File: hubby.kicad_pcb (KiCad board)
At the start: 2 copper layers, 70 x 100 mm, 79 parts, among them IC1 FE2.1, J1 USB1, J10 VPROG_OUT, J11 1V8_OUT, J12 VPROG_OUT, J13 USB2, J14 USB2, J15 UART_OUT, J17 EXT_PS_OUT, J18 EXT_PS_OUT, J2 USB2, J5 3V3_OUT, J6 1V8_OUT, J7 5V_OUT, J8 5V_OUT, J9 3V3_OUT, P1 USB_C_Plug_USB2.0, Q1 AO3401A, Q2 AO3401A, Q3 AO3401A, U1 USBLC6-2SC6, U10 TPS565208, U12 TPS565208, U13 AP1117-18, U14 AP1117-33, U15 USBLC6-2SC6, U16 USBLC6-2SC6, U17 USBLC6-2SC6, U18 USBLC6-2SC6, U19 INA181, U2 STM32F103RBTx, U3 INA181, U4 INA181, U5 INA181, U6 INA181, U7 FT2232HL, U8 INA181, U9 INA181, X1 ECS-2520MV-xxx-xx

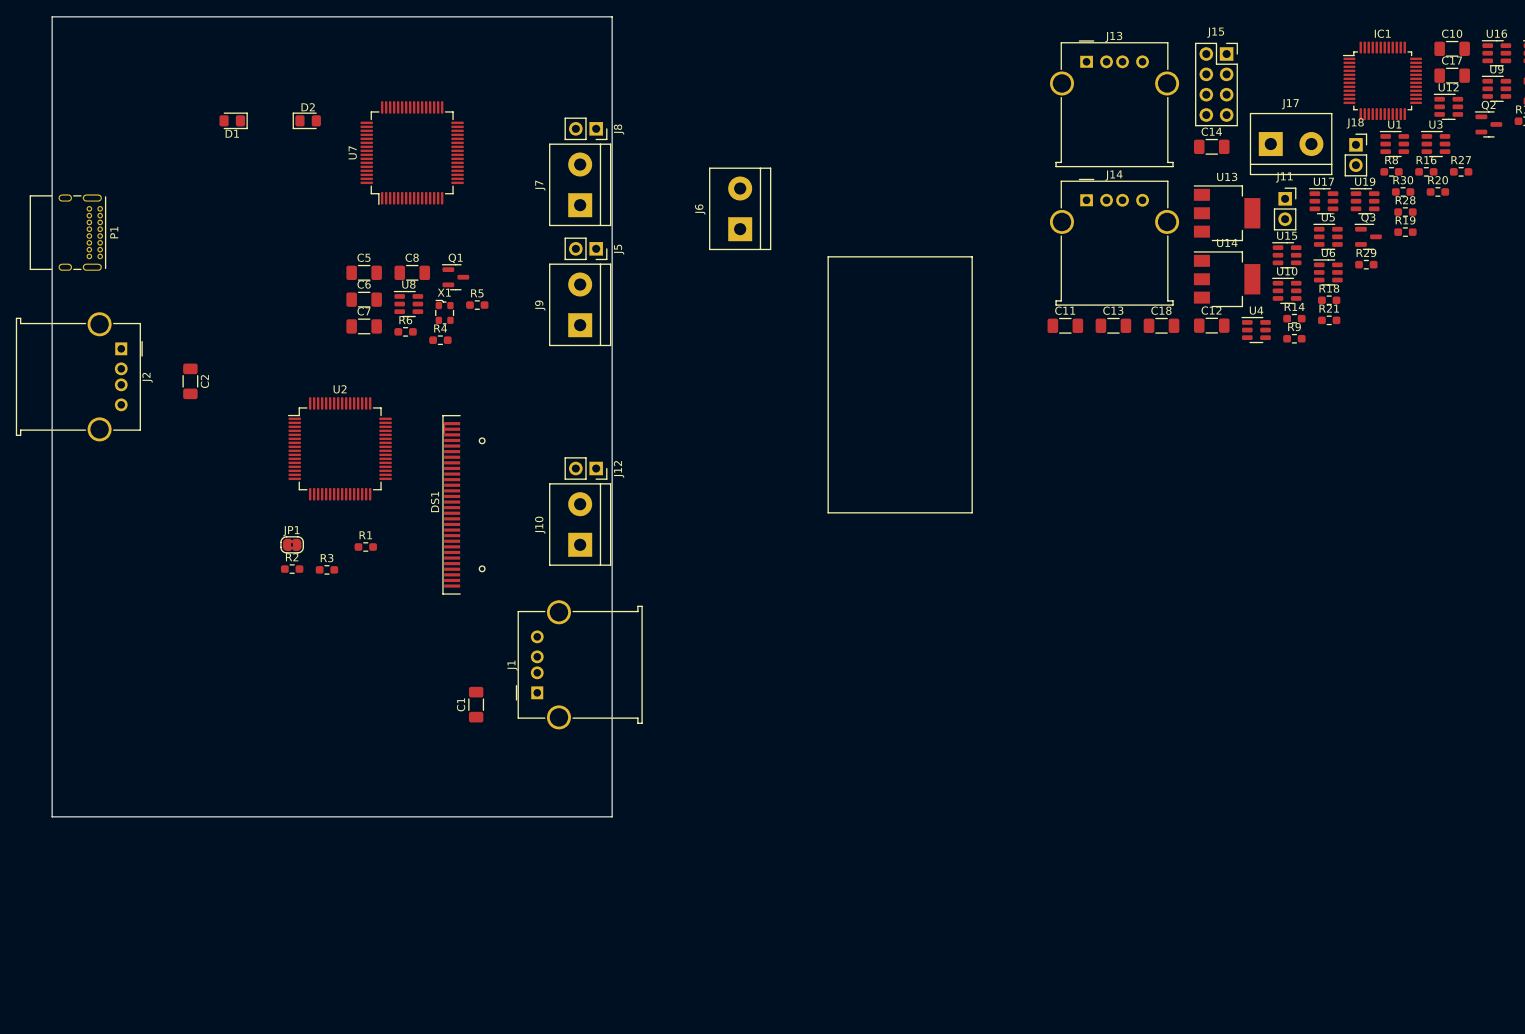
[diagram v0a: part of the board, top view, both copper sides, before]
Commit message: commiting cause i'm terrified of kicad 5.99
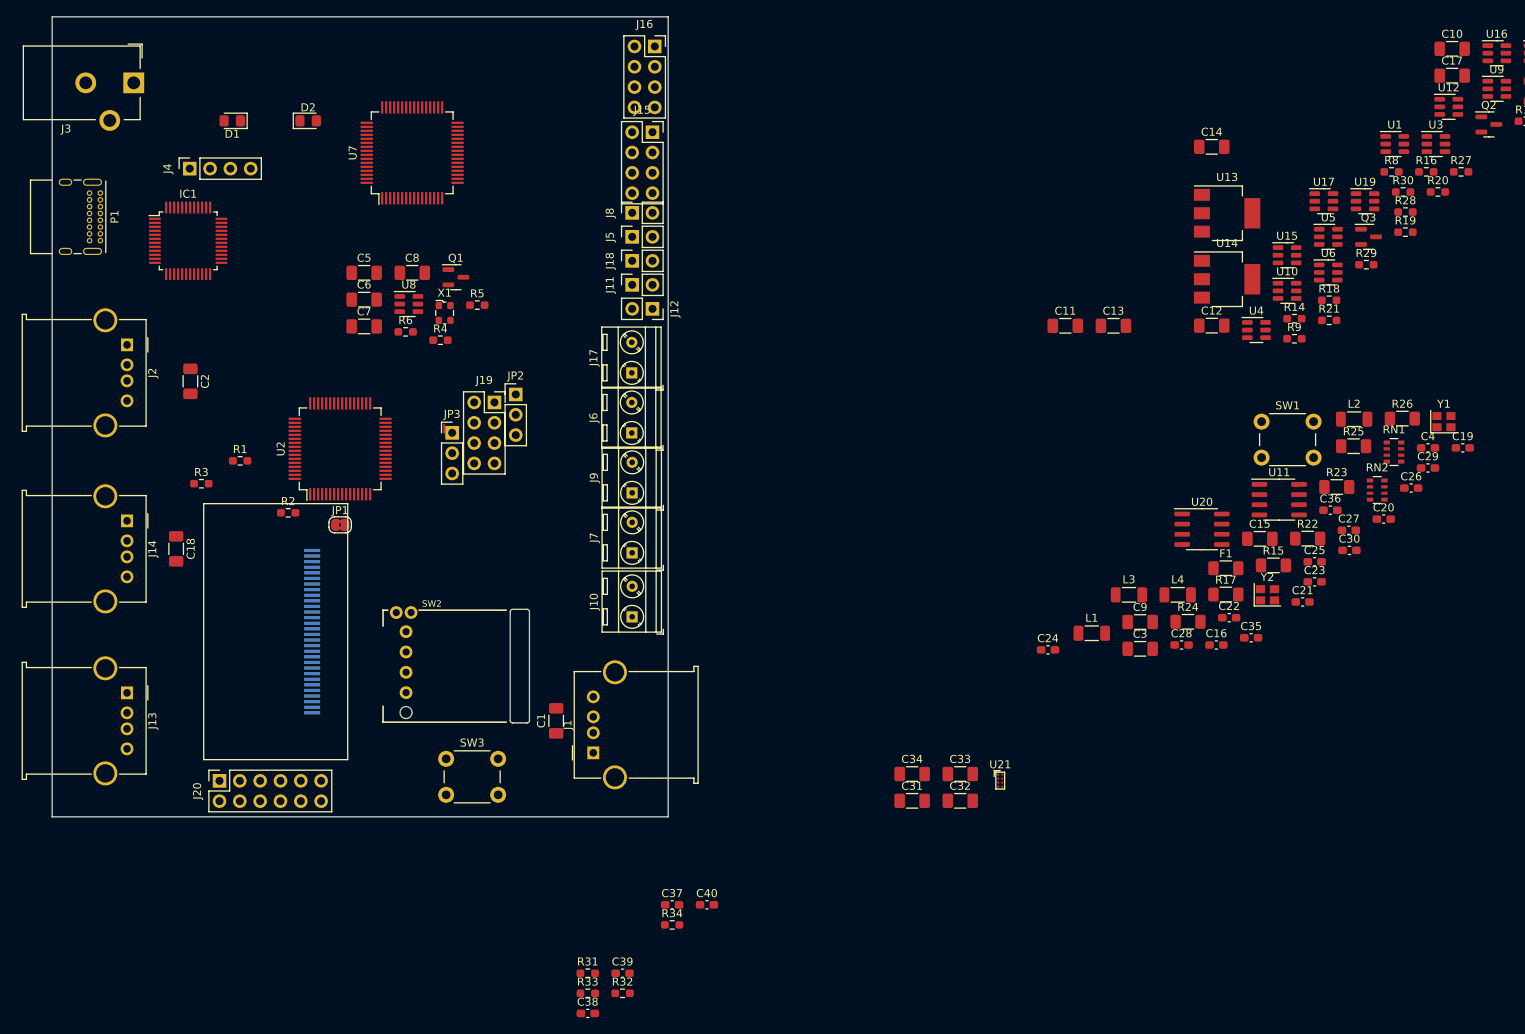
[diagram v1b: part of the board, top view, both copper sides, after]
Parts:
- added C15: C, Capacitor_SMD:C_1206_3216Metric_Pad1.33x1.80mm_HandSolder, F.Cu at (251.0, 95.2)
- added C16: 100n, Capacitor_SMD:C_0603_1608Metric_Pad1.08x0.95mm_HandSolder, F.Cu at (245.5, 108.5)
- added C19: 100n, Capacitor_SMD:C_0603_1608Metric_Pad1.08x0.95mm_HandSolder, F.Cu at (276.3, 83.9)
- added C20: 100n, Capacitor_SMD:C_0603_1608Metric_Pad1.08x0.95mm_HandSolder, F.Cu at (266.4, 92.8)
- added C21: 100n, Capacitor_SMD:C_0603_1608Metric_Pad1.08x0.95mm_HandSolder, F.Cu at (256.3, 103.1)
- added C22: 100n, Capacitor_SMD:C_0603_1608Metric_Pad1.08x0.95mm_HandSolder, F.Cu at (247.1, 105.1)
- added C23: 100n, Capacitor_SMD:C_0603_1608Metric_Pad1.08x0.95mm_HandSolder, F.Cu at (257.8, 100.6)
- added C24: 100n, Capacitor_SMD:C_0603_1608Metric_Pad1.08x0.95mm_HandSolder, F.Cu at (224.5, 109.1)
- added C25: 100n, Capacitor_SMD:C_0603_1608Metric_Pad1.08x0.95mm_HandSolder, F.Cu at (257.8, 98.1)
- added C26: 100n, Capacitor_SMD:C_0603_1608Metric_Pad1.08x0.95mm_HandSolder, F.Cu at (269.9, 88.9)
- added C27: 100n, Capacitor_SMD:C_0603_1608Metric_Pad1.08x0.95mm_HandSolder, F.Cu at (262.1, 94.2)
- added C28: 100n, Capacitor_SMD:C_0603_1608Metric_Pad1.08x0.95mm_HandSolder, F.Cu at (241.2, 108.5)
- added C29: 1n, Capacitor_SMD:C_0603_1608Metric_Pad1.08x0.95mm_HandSolder, F.Cu at (272.0, 86.4)
- added C3: C, Capacitor_SMD:C_1206_3216Metric_Pad1.33x1.80mm_HandSolder, F.Cu at (236.0, 109.0)
- added C30: 1n, Capacitor_SMD:C_0603_1608Metric_Pad1.08x0.95mm_HandSolder, F.Cu at (262.2, 96.7)
- added C31: 10u, Capacitor_SMD:C_1206_3216Metric_Pad1.33x1.80mm_HandSolder, F.Cu at (207.5, 128.0)
- added C32: 10u, Capacitor_SMD:C_1206_3216Metric_Pad1.33x1.80mm_HandSolder, F.Cu at (213.5, 128.0)
- added C33: 10u, Capacitor_SMD:C_1206_3216Metric_Pad1.33x1.80mm_HandSolder, F.Cu at (213.5, 124.7)
- added C34: 10u, Capacitor_SMD:C_1206_3216Metric_Pad1.33x1.80mm_HandSolder, F.Cu at (207.5, 124.7)
- added C35: 100n, Capacitor_SMD:C_0603_1608Metric_Pad1.08x0.95mm_HandSolder, F.Cu at (249.9, 107.6)
- added C36: 100n, Capacitor_SMD:C_0603_1608Metric_Pad1.08x0.95mm_HandSolder, F.Cu at (259.8, 91.7)
- added C37: 1n, Capacitor_SMD:C_0603_1608Metric_Pad1.08x0.95mm_HandSolder, F.Cu at (177.5, 141.0)
- added C38: 1n, Capacitor_SMD:C_0603_1608Metric_Pad1.08x0.95mm_HandSolder, F.Cu at (166.9, 154.6)
- added C39: 1n, Capacitor_SMD:C_0603_1608Metric_Pad1.08x0.95mm_HandSolder, F.Cu at (171.3, 149.6)
- added C4: 100n, Capacitor_SMD:C_0603_1608Metric_Pad1.08x0.95mm_HandSolder, F.Cu at (272.0, 83.9)
- added C40: 1n, Capacitor_SMD:C_0603_1608Metric_Pad1.08x0.95mm_HandSolder, F.Cu at (181.8, 141.0)
- added C9: C, Capacitor_SMD:C_1206_3216Metric_Pad1.33x1.80mm_HandSolder, F.Cu at (236.0, 105.7)
- added F1: Polyfuse, Resistor_SMD:R_1206_3216Metric_Pad1.30x1.75mm_HandSolder, F.Cu at (246.7, 98.9)
- added J16: JTAG_OUT, Connector_PinSocket_2.54mm:PinSocket_2x04_P2.54mm_Vertical, F.Cu at (175.3, 33.7)
- added J19: STM_PROG_ENA, Connector_PinSocket_2.54mm:PinSocket_2x04_P2.54mm_Vertical, F.Cu at (155.3, 78.2)
- added J20: STM_EXT_IO, Connector_PinSocket_2.54mm:PinSocket_2x06_P2.54mm_Vertical, F.Cu at (120.9, 125.5)
- added J3: Barrel_Jack_Switch, Connector_BarrelJack:BarrelJack_CUI_PJ-102AH_Horizontal, F.Cu at (110.2, 38.2)
- added J4: Conn_01x04, Connector_PinSocket_2.54mm:PinSocket_1x04_P2.54mm_Vertical, F.Cu at (117.2, 49.0)
- added JP2: TDO_VSHIFT, Connector_PinHeader_2.54mm:PinHeader_1x03_P2.54mm_Vertical, F.Cu at (157.9, 77.2)
- added JP3: RXD_VSHIFT, Connector_PinHeader_2.54mm:PinHeader_1x03_P2.54mm_Vertical, F.Cu at (150.0, 82.0)
- added L1: L, Inductor_SMD:L_1206_3216Metric_Pad1.22x1.90mm_HandSolder, F.Cu at (229.9, 107.0)
- added L2: L, Inductor_SMD:L_1206_3216Metric_Pad1.22x1.90mm_HandSolder, F.Cu at (262.8, 80.3)
- added L3: L, Inductor_SMD:L_1206_3216Metric_Pad1.22x1.90mm_HandSolder, F.Cu at (234.6, 102.2)
- added L4: L, Inductor_SMD:L_1206_3216Metric_Pad1.22x1.90mm_HandSolder, F.Cu at (240.7, 102.2)
- added R15: 0.5R, Resistor_SMD:R_1206_3216Metric_Pad1.30x1.75mm_HandSolder, F.Cu at (252.7, 98.6)
- added R17: 0.5R, Resistor_SMD:R_1206_3216Metric_Pad1.30x1.75mm_HandSolder, F.Cu at (246.7, 102.2)
- added R22: 0.5R, Resistor_SMD:R_1206_3216Metric_Pad1.30x1.75mm_HandSolder, F.Cu at (256.9, 95.2)
- added R23: 0.5R, Resistor_SMD:R_1206_3216Metric_Pad1.30x1.75mm_HandSolder, F.Cu at (260.6, 88.8)
- added R24: 0.5R, Resistor_SMD:R_1206_3216Metric_Pad1.30x1.75mm_HandSolder, F.Cu at (242.0, 105.6)
- added R25: 0.5R, Resistor_SMD:R_1206_3216Metric_Pad1.30x1.75mm_HandSolder, F.Cu at (262.7, 83.7)
- added R26: 0.5R, Resistor_SMD:R_1206_3216Metric_Pad1.30x1.75mm_HandSolder, F.Cu at (268.8, 80.2)
- added R31: 100k, Resistor_SMD:R_0603_1608Metric_Pad0.98x0.95mm_HandSolder, F.Cu at (166.9, 149.6)
- added R32: 100k, Resistor_SMD:R_0603_1608Metric_Pad0.98x0.95mm_HandSolder, F.Cu at (171.3, 152.1)
- added R33: 100k, Resistor_SMD:R_0603_1608Metric_Pad0.98x0.95mm_HandSolder, F.Cu at (166.9, 152.1)
- added R34: 100k, Resistor_SMD:R_0603_1608Metric_Pad0.98x0.95mm_HandSolder, F.Cu at (177.5, 143.5)
- added RN1: 22, Resistor_SMD:R_Array_Convex_4x0603, F.Cu at (267.7, 84.4)
- added RN2: 22, Resistor_SMD:R_Array_Convex_4x0603, F.Cu at (265.6, 89.2)
- added SW1: SW_Push, Button_Switch_THT:SW_PUSH_6mm_H4.3mm, F.Cu at (251.2, 80.6)
- added SW2: KB_ENC, Critbit_lib:RollerEncoder_Panasonic_EVQWGD001, F.Cu at (149.9, 110.7)
- added SW3: BUT_BACK, Button_Switch_THT:SW_PUSH_6mm_H4.3mm, F.Cu at (149.2, 122.8)
- added U11: 24LC00, Package_SO:SOIC-8_3.9x4.9mm_P1.27mm, F.Cu at (253.4, 90.3)
- added U20: 24LC00, Package_SO:SOIC-8_3.9x4.9mm_P1.27mm, F.Cu at (243.7, 94.0)
- added U21: SN74LVC2T45YZP, Package_BGA:Texas_DSBGA-8_0.9x1.9mm_Layout2x4_P0.5mm, F.Cu at (218.5, 125.5)
- added Y1: 6MHZ 2520, Crystal:Crystal_SMD_2520-4Pin_2.5x2.0mm, F.Cu at (274.0, 80.6)
- added Y2: 6MHZ 2520, Crystal:Crystal_SMD_2520-4Pin_2.5x2.0mm, F.Cu at (251.9, 102.2)
- DS1: moved to B.Cu
- J10, J17, J6, J7, J9: footprint TerminalBlock:TerminalBlock_bornier-2_P5.08mm -> TerminalBlock_MetzConnect:TerminalBlock_MetzConnect_Type086_RT03402HBLC_1x02_P3.81mm_Horizontal
- moved IC1 150.7 mm to (117.0, 58.0)
- moved J13 143.6 mm to (109.4, 114.5), turned to -90 degrees
- moved J14 126.5 mm to (109.4, 93.0), turned to -90 degrees
- moved C18 126.3 mm to (115.5, 96.5), turned to -90 degrees
- moved J18 91.6 mm to (172.5, 60.5), turned to 90 degrees
- moved J17 84.8 mm to (172.5, 74.5), turned to 90 degrees
- moved J11 82.3 mm to (172.5, 63.5), turned to 90 degrees
- moved J15 72.4 mm to (175.0, 44.4)
- moved J7 43.9 mm to (172.5, 97.0)
- moved J6 28.9 mm to (172.5, 82.0)
- moved DS1 23.6 mm to (132.5, 106.8), turned to 90 degrees
- moved J9 21.9 mm to (172.5, 89.5)
- moved J12 21.2 mm to (175.0, 66.5)
- moved R1 19.0 mm to (123.5, 85.5)
- moved R3 19.0 mm to (118.7, 88.4)
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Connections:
- IC1 pad 22: unconnected-(IC1-Pad22) -> Net-(C31-Pad1)
- IC1 pad 23: unconnected-(IC1-Pad23) -> Net-(C32-Pad1)
- J15 pad 2: /RTS -> /TARG_RTS
- J15 pad 3: /DTR -> /TARG_DTR
- J15 pad 4: /RXD -> /TARG_TXD
- J15 pad 8: /TXD -> /TARG_RXD
- JP1 pad 1: /TDI -> /TDO
- R2 pad 2: /TDO -> /TDI
- U2 pad 10: unconnected-(U2-Pad10) -> /ADC_???
- U2 pad 12: Net-(U2-Pad12) -> GND
- U2 pad 18: Net-(U2-Pad12) -> GND
- U2 pad 24: unconnected-(U2-Pad24) -> /STM_PROBE1
- U2 pad 25: unconnected-(U2-Pad25) -> /STM_PROBE2
- U2 pad 26: /5V_CURR -> /EXT_IO1
- U2 pad 27: unconnected-(U2-Pad27) -> /EXT_IO2
- U2 pad 28: unconnected-(U2-Pad28) -> /EXT_IO3
- U2 pad 29: unconnected-(U2-Pad29) -> /EXT_IO4
- U2 pad 30: unconnected-(U2-Pad30) -> /EXT_IO5
- U2 pad 31: Net-(U2-Pad12) -> GND
- U2 pad 37: unconnected-(U2-Pad37) -> /VPROG_PWM
- U2 pad 41: /VPROG_PWM -> /STM32_CLK_OUT
- U2 pad 42: unconnected-(U2-Pad42) -> /STM_TXD
- U2 pad 43: unconnected-(U2-Pad43) -> /STM_RXD
- U2 pad 44: unconnected-(U2-Pad44) -> /STM32_DM
- U2 pad 45: unconnected-(U2-Pad45) -> /STM32_DP
- U2 pad 47: Net-(U2-Pad12) -> GND
- U2 pad 5: unconnected-(U2-Pad5) -> /STM32_12MHZ
- U2 pad 50: unconnected-(U2-Pad50) -> /STM_PULSE_CNT
- U2 pad 54: unconnected-(U2-Pad54) -> /OLED_RST
- U2 pad 55: unconnected-(U2-Pad55) -> /OLED_CLK
- U2 pad 56: unconnected-(U2-Pad56) -> /OLED_CS
- U2 pad 57: unconnected-(U2-Pad57) -> /OLED_MOSI
- U2 pad 58: unconnected-(U2-Pad58) -> /ENC_A
- U2 pad 59: unconnected-(U2-Pad59) -> /ENC_B
- U2 pad 60: unconnected-(U2-Pad60) -> GND
- U2 pad 61: unconnected-(U2-Pad61) -> /ENC_BUT
- U2 pad 62: unconnected-(U2-Pad62) -> /STM_BUT_BACK
- U2 pad 63: Net-(U2-Pad12) -> GND
- U2 pad 7: unconnected-(U2-Pad7) -> /STM_BUT_RST
- U2 pad 8: unconnected-(U2-Pad8) -> /5V_CURR
- U2 pad 9: unconnected-(U2-Pad9) -> /USB1_CURR
- U7 pad 2: unconnected-(U7-Pad2) -> Net-(C33-Pad1)
- U7 pad 3: unconnected-(U7-Pad3) -> Net-(C34-Pad1)
- U7 pad 4: Net-(U7-Pad4) -> Net-(C26-Pad1)
- U7 pad 9: Net-(U7-Pad4) -> Net-(C35-Pad1)
- X1 pad 2: unconnected-(X1-Pad2) -> GND
- X1 pad 3: unconnected-(X1-Pad3) -> /STM32_12MHZ
- X1 pad 4: unconnected-(X1-Pad4) -> +3V3
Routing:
- net Net-(C5-Pad1): track 1.00 -> 0.00 mm
- net GND: track 0.00 -> 1.00 mm
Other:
- board size 70 x 100 mm -> 77 x 100 mm
- board text added: "target stackup - JLC7628 HI-SPD1 0.2 mm GND 0.465 mm HI-SPD2/PWR 0.2 mm LO-SPD USB 90R: OUT - .7mm/.4mm IN - .5/.4mm"

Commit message: another progress checkpoint
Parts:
- removed DS1: OLED-128O064D, Display:OLED-128O064D
- removed J10: VPROG_OUT, TerminalBlock_MetzConnect:TerminalBlock_MetzConnect_Type086_RT03402HBLC_1x02_P3.81mm_Horizontal
- removed J11: 1V8_OUT, Connector_PinSocket_2.54mm:PinSocket_1x02_P2.54mm_Vertical
- removed J12: VPROG_OUT, Connector_PinSocket_2.54mm:PinSocket_1x02_P2.54mm_Vertical
- removed J15: UART_OUT, Connector_PinSocket_2.54mm:PinSocket_2x04_P2.54mm_Vertical
- removed J17: EXT_PS_OUT, TerminalBlock_MetzConnect:TerminalBlock_MetzConnect_Type086_RT03402HBLC_1x02_P3.81mm_Horizontal
- removed J18: EXT_PS_OUT, Connector_PinSocket_2.54mm:PinSocket_1x02_P2.54mm_Vertical
- removed J8: 5V_OUT, Connector_PinSocket_2.54mm:PinSocket_1x02_P2.54mm_Vertical
- removed J9: 3V3_OUT, TerminalBlock_MetzConnect:TerminalBlock_MetzConnect_Type086_RT03402HBLC_1x02_P3.81mm_Horizontal
- added C41: 10u/16V, Capacitor_SMD:C_1206_3216Metric_Pad1.33x1.80mm_HandSolder, F.Cu at (198.0, 50.5)
- added C42: 220u, Capacitor_THT:C_Radial_D10.0mm_H12.5mm_P5.00mm, F.Cu at (161.2, 47.0)
- added C43: 1n, Capacitor_SMD:C_0603_1608Metric_Pad1.08x0.95mm_HandSolder, F.Cu at (117.0, 154.0)
- added C44: 1n, Capacitor_SMD:C_0603_1608Metric_Pad1.08x0.95mm_HandSolder, F.Cu at (112.7, 159.0)
- added C45: 10u, Capacitor_SMD:C_1206_3216Metric_Pad1.33x1.80mm_HandSolder, F.Cu at (153.0, 179.0)
- added C46: 10u, Capacitor_SMD:C_1206_3216Metric_Pad1.33x1.80mm_HandSolder, F.Cu at (143.2, 187.2)
- added J21: Conn_01x08, Connector_PinSocket_2.54mm:PinSocket_1x08_P2.54mm_Vertical, F.Cu at (129.1, 106.0)
- added R35: 0R, Resistor_SMD:R_0603_1608Metric_Pad0.98x0.95mm_HandSolder, F.Cu at (142.9, 138.7)
- added R36: 100k, Resistor_SMD:R_0603_1608Metric_Pad0.98x0.95mm_HandSolder, F.Cu at (112.7, 154.0)
- added R37: 100k, Resistor_SMD:R_0603_1608Metric_Pad0.98x0.95mm_HandSolder, F.Cu at (112.7, 156.5)
- added U22: AP1117-33, Package_TO_SOT_SMD:SOT-223-3_TabPin2, F.Cu at (145.1, 181.4)
- J16: footprint Connector_PinSocket_2.54mm:PinSocket_2x04_P2.54mm_Vertical -> Connector_PinHeader_2.54mm:PinHeader_2x04_P2.54mm_Horizontal
- J19: footprint Connector_PinSocket_2.54mm:PinSocket_2x04_P2.54mm_Vertical -> Connector_PinHeader_2.54mm:PinHeader_2x04_P2.54mm_Vertical
- J20: footprint Connector_PinSocket_2.54mm:PinSocket_2x06_P2.54mm_Vertical -> Connector_PinHeader_2.54mm:PinHeader_2x06_P2.54mm_Horizontal
- J5: value 3V3_OUT -> Screw_Terminal_01x10; footprint Connector_PinSocket_2.54mm:PinSocket_1x02_P2.54mm_Vertical -> TerminalBlock_Phoenix:TerminalBlock_Phoenix_MKDS-1,5-10-5.08_1x10_P5.08mm_Horizontal
- J6: value 1V8_OUT -> Conn_02x06_Odd_Even; footprint TerminalBlock_MetzConnect:TerminalBlock_MetzConnect_Type086_RT03402HBLC_1x02_P3.81mm_Horizontal -> Connector_PinHeader_2.54mm:PinHeader_2x06_P2.54mm_Horizontal
- J7: value 5V_OUT -> UART_OUT; footprint TerminalBlock_MetzConnect:TerminalBlock_MetzConnect_Type086_RT03402HBLC_1x02_P3.81mm_Horizontal -> Connector_PinHeader_2.54mm:PinHeader_2x04_P2.54mm_Horizontal
- R4: value 10k -> 100k
- R5: value 10k -> DNP
- SW2: value KB_ENC -> RotaryEncoder_Switch; footprint Critbit_lib:RollerEncoder_Panasonic_EVQWGD001 -> Rotary_Encoder:RotaryEncoder_Alps_EC12E-Switch_Vertical_H20mm_CircularMountingHoles
- SW3: value BUT_BACK -> RotaryEncoder_Switch; footprint Button_Switch_THT:SW_PUSH_6mm_H4.3mm -> Rotary_Encoder:RotaryEncoder_Alps_EC12E-Switch_Vertical_H20mm_CircularMountingHoles
- moved SW1 132.5 mm to (119.8, 97.8)
- moved R4 91.2 mm to (138.3, 161.1)
- moved R5 72.9 mm to (147.3, 138.7)
- moved C7 68.4 mm to (204.1, 47.7)
- moved C5 68.3 mm to (204.0, 41.0)
- moved C6 63.8 mm to (198.0, 41.0)
- moved C8 61.7 mm to (204.1, 44.4)
- moved J20 61.4 mm to (165.8, 83.7), turned to 0 degrees
- moved J6 34.7 mm to (165.8, 47.9), turned to 0 degrees
- moved J16 31.0 mm to (165.8, 63.1)
- moved J5 25.6 mm to (160.9, 34.7), turned to 180 degrees
- moved SW3 25.4 mm to (124.5, 128.2), turned to 90 degrees
- moved J7 24.4 mm to (165.8, 73.5), turned to 0 degrees
- moved SW2 18.1 mm to (145.5, 128.2), turned to 90 degrees
- moved J3 5.75 mm to (110.2, 44.0)
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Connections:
- net /ENC_BUT renamed /STM_BUT1
- net /ENC_SW renamed Net-(C40-Pad1)
- net /STM32_12MHZ renamed /STM_12MHZ
- net /STM32_CLK_OUT renamed /STM_CLK_OUT
- net /STM32_DM renamed /STM_DM
- net /STM32_DP renamed /STM_DP
- C19 pad 1: +3V3 -> VDDA
- C20 pad 1: +3V3 -> VDDA
- C21 pad 1: +3V3 -> VDDA
- C22 pad 1: +3V3 -> VDDA
- C23 pad 1: +3V3 -> VDDA
- C27 pad 1: +3V3 -> VDD
- C30 pad 1: +3V3 -> VDD
- C37 pad 1: /STM_BUT_BACK -> Net-(C37-Pad1)
- C38 pad 1: /ENC_A -> Net-(C38-Pad1)
- C39 pad 1: /ENC_B -> Net-(C39-Pad1)
- C5 pad 1: Net-(C5-Pad1) -> /5V_OUT
- C5 pad 2: Net-(C5-Pad2) -> GND
- C6 pad 1: Net-(C6-Pad1) -> /3V3_OUT
- C6 pad 2: Net-(C6-Pad2) -> GND
- C7 pad 1: GND -> /1V8_OUT
- C7 pad 2: Net-(C7-Pad2) -> GND
- C8 pad 1: Net-(C8-Pad1) -> /VPROG_OUT
- IC1 pad 15: +3V3 -> VDD
- IC1 pad 20: +3V3 -> VDD
- IC1 pad 26: +3V3 -> VDD
- IC1 pad 31: +3V3 -> VDD
- IC1 pad 36: +3V3 -> VDD
- IC1 pad 42: +3V3 -> VDD
- J20 pad 1: GND -> /STM_PROBE1
- J20 pad 11: GND -> /VPROG_OUT
- J20 pad 12: +VSW -> unconnected-(J20-Pad12)
- J20 pad 2: /STM_PROBE1 -> unconnected-(J20-Pad2)
- J20 pad 3: GND -> /STM_PROBE2
- J20 pad 4: /STM_PROBE2 -> unconnected-(J20-Pad4)
- J5 pad 1: Net-(J5-Pad1) -> /EXT_PS_OUT
- J6 pad 1: Net-(J11-Pad1) -> /EXT_PS_OUT
- J7 pad 1: Net-(J7-Pad1) -> /UART_3V3
- J7 pad 2: GND -> /UART_5V
- L3 pad 1: +3V3 -> VDD
- L4 pad 1: +3V3 -> VDD
- Q2 pad 1: /VBUS_SUCC_ENA -> /EXT_PS_DET
- R1 pad 2: +3V3 -> VDD
- R22 pad 2: Net-(J7-Pad1) -> /5V_OUT
- R23 pad 2: Net-(J5-Pad1) -> /3V3_OUT
- R24 pad 2: Net-(J11-Pad1) -> /1V8_OUT
- R25 pad 2: Net-(J10-Pad1) -> /VPROG_OUT
- R26 pad 2: Net-(J17-Pad1) -> /EXT_PS_OUT
- R28 pad 2: +3V3 -> VDD
- R29 pad 2: +3V3 -> VDD
- R3 pad 2: +3V3 -> VDD
- R31 pad 1: /STM_BUT_BACK -> Net-(C37-Pad1)
- R31 pad 2: +3V3 -> VDD
- R32 pad 1: /ENC_A -> Net-(C38-Pad1)
- R32 pad 2: +3V3 -> VDD
- R33 pad 1: /ENC_B -> Net-(C39-Pad1)
- R33 pad 2: +3V3 -> VDD
- R34 pad 2: +3V3 -> VDD
- R4 pad 1: /OLED_RST -> GND
- R4 pad 2: +3V3 -> /LCD_RST
- R5 pad 1: Net-(DS1-Pad15) -> /BOOT0
- R5 pad 2: +3V3 -> VDD
- R9 pad 1: /VBUS_SUCC_ENA -> /EXT_PS_DET
- SW2 pad A: /ENC_A -> Net-(C38-Pad1)
- SW2 pad B: /ENC_B -> Net-(C39-Pad1)
- U11 pad 8: +3V3 -> VDD
- U19 pad 4: Net-(J17-Pad1) -> /EXT_PS_OUT
- U19 pad 6: +3V3 -> VDDA
- U2 pad 1: +3V3 -> VDD
- U2 pad 10: /ADC_??? -> /VPROG_OUT_CURR
- U2 pad 13: +3V3 -> VDDA
- U2 pad 14: /5V_VLT -> /VPROG_PWM
- U2 pad 15: /VPROG_VLT -> /5V_VLT
- U2 pad 16: /EXT_PS_VLT -> /VPROG_VLT
- U2 pad 17: /EXT_PS_OUT_CURR -> /EXT_PS_VLT
- U2 pad 19: +3V3 -> VDD
- U2 pad 20: /5V_OUT_CURR -> /EXT_PS_OUT_CURR
- U2 pad 21: /3V3_OUT_CURR -> /5V_OUT_CURR
- U2 pad 22: /1V8_OUT_CURR -> /3V3_OUT_CURR
- U2 pad 23: /VPROG_OUT_CURR -> /1V8_OUT_CURR
- U2 pad 32: +3V3 -> VDD
- U2 pad 37: /VPROG_PWM -> unconnected-(U2-Pad37)
- U2 pad 48: +3V3 -> VDD
- U2 pad 52: unconnected-(U2-Pad52) -> /LCD_BL
- U2 pad 53: unconnected-(U2-Pad53) -> /LCD_DC
- U2 pad 54: /OLED_RST -> /LCD_RST
- U2 pad 55: /OLED_CLK -> /LCD_CLK
- U2 pad 56: /OLED_CS -> /LCD_CS
- U2 pad 57: /OLED_MOSI -> /LCD_MOSI
- U2 pad 58: /ENC_A -> /ENC1_A
- U2 pad 59: /ENC_B -> /ENC1_B
- U2 pad 60: GND -> /BOOT0
- U2 pad 62: /STM_BUT_BACK -> /STM_BUT2
- U2 pad 64: +3V3 -> VDD
- U20 pad 8: +3V3 -> VDD
- U4 pad 4: Net-(J7-Pad1) -> /5V_OUT
- U4 pad 6: +3V3 -> VDDA
- U5 pad 4: Net-(J5-Pad1) -> /3V3_OUT
- U5 pad 6: +3V3 -> VDDA
- U6 pad 4: Net-(J11-Pad1) -> /1V8_OUT
- U6 pad 6: +3V3 -> VDDA
- U7 pad 20: /VCCIO_SEL -> VDD
- U7 pad 31: /VCCIO_SEL -> VDD
- U7 pad 42: /VCCIO_SEL -> VDD
- U7 pad 50: +3V3 -> VDD
- U7 pad 56: /VCCIO_SEL -> VDD
- U9 pad 4: Net-(J10-Pad1) -> /VPROG_OUT
- U9 pad 6: +3V3 -> VDDA
- X1 pad 4: +3V3 -> VDD
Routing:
- net (no net): vias 0 -> 4
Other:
- outline, holes or cut-outs redrawn
- copper layers 2 -> 4
